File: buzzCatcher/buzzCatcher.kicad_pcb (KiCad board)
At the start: 2 copper layers, 150 x 100 mm, 30 parts, among them IC1 CD4043BE-NG, IC2 COM-16473, IC3 CD74HCT173E, IC4 CD4072BE, IC5 SN74LS04N, IC6 SN74LS21NE4, J1 154-UL6661, J2 154-UL6661, J3 154-UL6661, J4 154-UL6661, J5 USB4130-GF-C, Q1 BS170, SW1 SW_Push

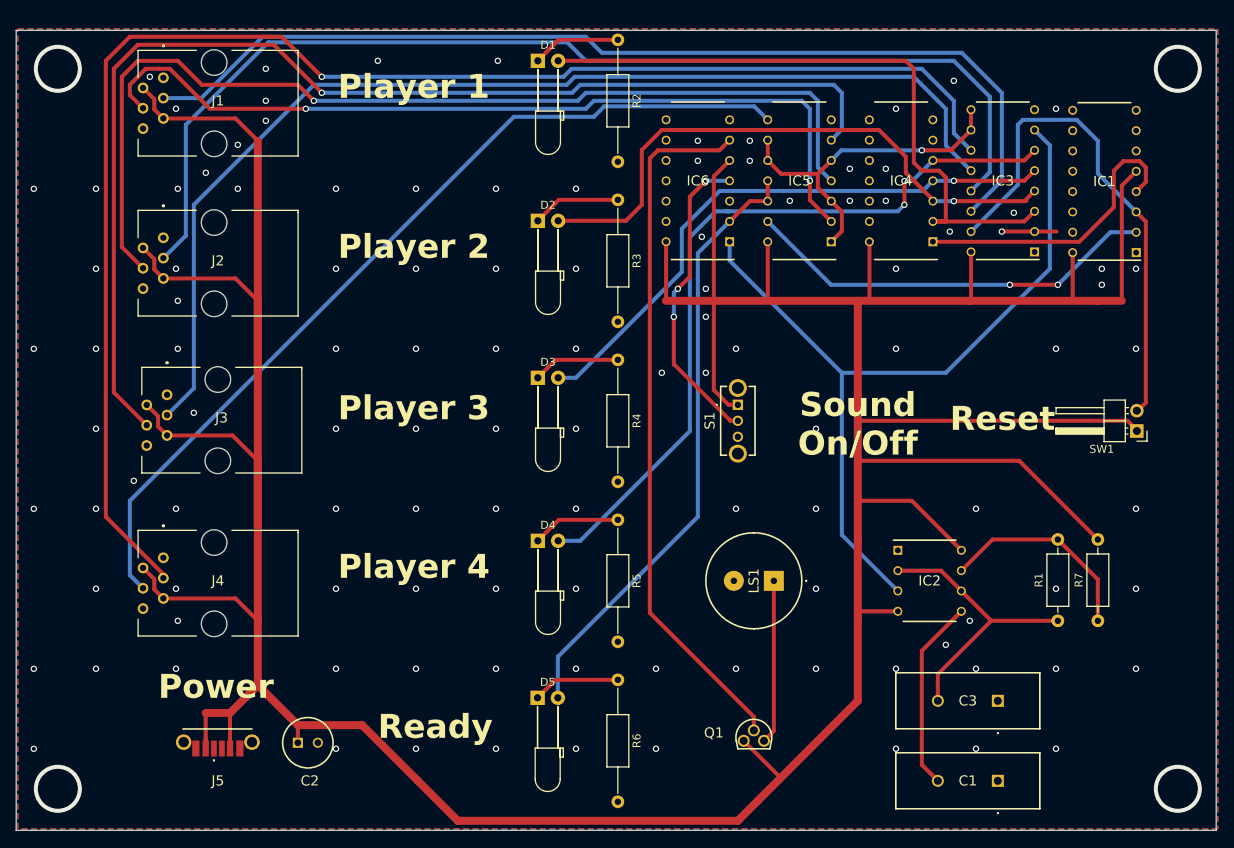
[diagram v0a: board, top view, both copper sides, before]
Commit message: Smaller and cheaper
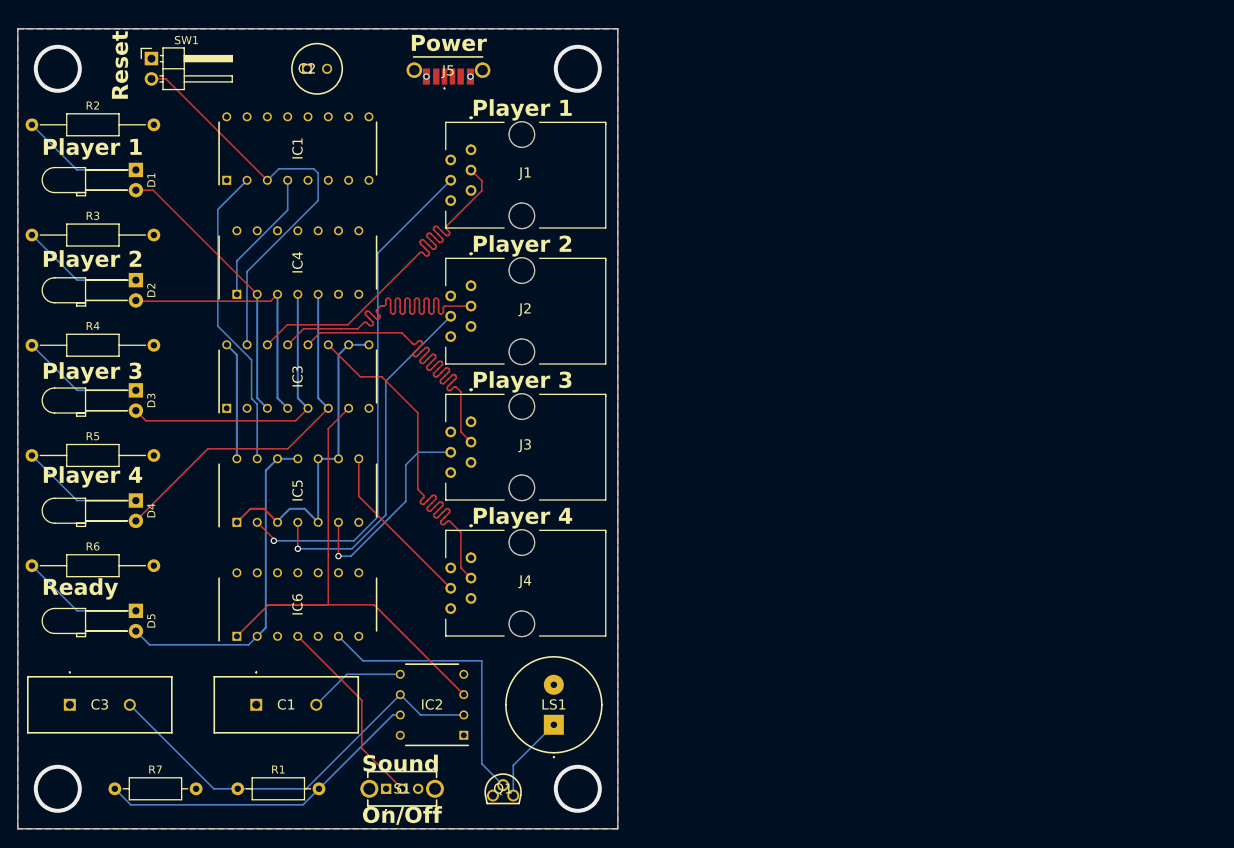
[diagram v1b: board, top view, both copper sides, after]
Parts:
- moved SW1 131.7 mm to (66.7, 53.7), turned to 0 degrees
- moved R7 124.7 mm to (62.1, 145.0), turned to 0 degrees
- moved C3 116.0 mm to (56.5, 134.5), turned to 0 degrees
- moved R1 104.6 mm to (77.5, 145.0), turned to 0 degrees
- moved IC1 100.9 mm to (85.0, 65.0), turned to 90 degrees
- moved C1 93.2 mm to (79.8, 134.5), turned to 0 degrees
- moved IC3 91.5 mm to (85.0, 93.5), turned to 90 degrees
- moved J5 88.8 mm to (103.8, 55.0)
- moved C2 84.3 mm to (86.2, 55.0)
- moved IC4 76.1 mm to (85.0, 79.2), turned to 90 degrees
- moved R6 74.6 mm to (51.8, 117.1), turned to 0 degrees
- moved R2 74.0 mm to (51.8, 62.0), turned to 0 degrees
- moved IC5 73.7 mm to (85.0, 107.7), turned to 90 degrees
- moved R5 73.7 mm to (51.8, 103.3), turned to 0 degrees
- moved R3 73.4 mm to (51.8, 75.8), turned to 0 degrees
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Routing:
- net /Vbus_5V: track 565.0 -> 14.8 mm
- net /trigger_4: track 186.1 -> 49.8 mm, vias 1 -> 0
- net Net-(IC5-3Y): track 148.3 -> 26.3 mm
- net Net-(IC5-4Y): track 112.5 -> 20.9 mm
- net /trigger_3: track 139.0 -> 49.8 mm
- net /trigger_2: track 138.2 -> 50.2 mm
- net Net-(IC5-2Y): track 126.4 -> 44.2 mm
- net /trigger_1: track 127.3 -> 49.8 mm
- net Net-(IC6-1Y): track 87.8 -> 35.8 mm
- net Net-(D4-A): track 96.2 -> 44.7 mm, vias 2 -> 0
- net Net-(D1-A): track 81.7 -> 35.3 mm
- net Net-(IC5-1Y): track 107.5 -> 63.3 mm, vias 2 -> 1
- net Net-(D2-A): track 73.6 -> 33.3 mm, vias 1 -> 0
- net Net-(D3-A): track 73.4 -> 37.5 mm, vias 1 -> 0
- net /listening: track 76.8 -> 42.1 mm
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- added copper zone on F.Cu, net /Vbus_5V
- removed copper zone on F.Cu, net GND
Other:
- board size 150 x 100 mm -> 75 x 100 mm

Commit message: More compact draft
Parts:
- moved IC2 32.9 mm to (70.0, 143.0), turned to 90 degrees
- moved Q1 26.7 mm to (82.7, 145.3)
- moved LS1 19.0 mm to (98.0, 138.0)
- moved S1 17.1 mm to (81.5, 136.0)
- moved R1 17.1 mm to (64.4, 134.0)
- moved R7 15.3 mm to (51.4, 134.0)
- moved J1 11.5 mm to (95.2, 65.6)
- moved J2 11.5 mm to (95.2, 82.6)
- moved J3 11.5 mm to (95.2, 99.6)
- moved J4 11.5 mm to (95.2, 116.6)
- moved J5 8.83 mm to (95.0, 54.8)
- moved IC6 8.82 mm to (79.0, 115.5)
- moved C1 8.56 mm to (76.8, 126.5)
- moved C3 8.00 mm to (56.5, 126.5)
- moved IC5 7.63 mm to (79.0, 103.0)
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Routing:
- net GND: track 0.00 -> 60.0 mm, vias 6 -> 22
- net Net-(IC2-THRES): track 52.0 -> 25.6 mm
- net Net-(IC5-2Y): track 44.2 -> 26.2 mm, vias 1 -> 0
- net Net-(IC5-1Y): track 63.3 -> 45.3 mm, vias 1 -> 0
- net Net-(IC5-3Y): track 26.3 -> 10.0 mm, vias 1 -> 0
- net /Vbus_5V: track 14.8 -> 0.00 mm
- net Net-(IC2-DISCH): track 41.2 -> 27.5 mm
- net Net-(IC1-S1): track 16.9 -> 26.7 mm
- net Net-(IC5-4Y): track 20.9 -> 29.4 mm
- net Net-(IC2-OUT): track 67.7 -> 59.3 mm
- net Net-(D3-A): track 37.5 -> 29.6 mm
- net /listening_state*: track 38.4 -> 31.0 mm
- net /reset_button: track 52.0 -> 44.8 mm
- net Net-(D4-A): track 44.7 -> 37.5 mm
- net Net-(IC6-1Y): track 35.8 -> 29.1 mm
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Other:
- board size 75 x 100 mm -> 63 x 100 mm

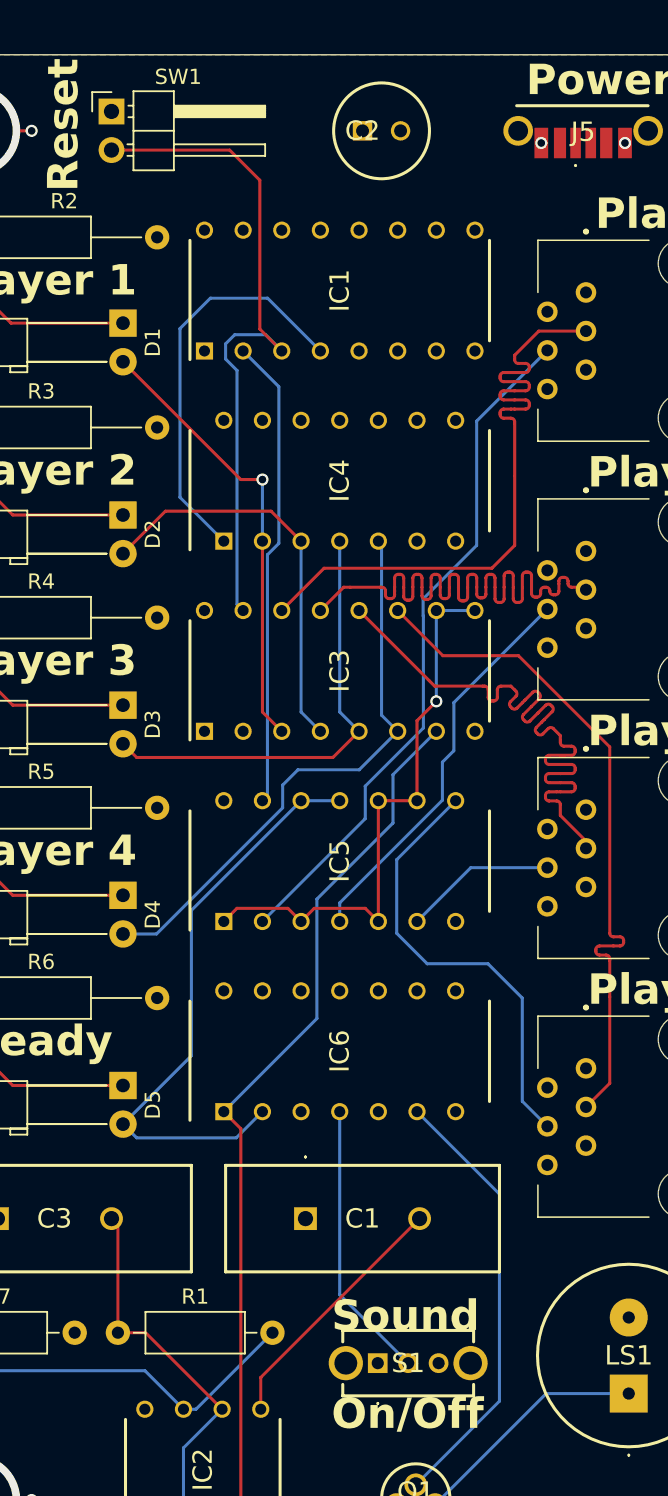
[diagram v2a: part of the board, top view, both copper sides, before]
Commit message: Added handle parts
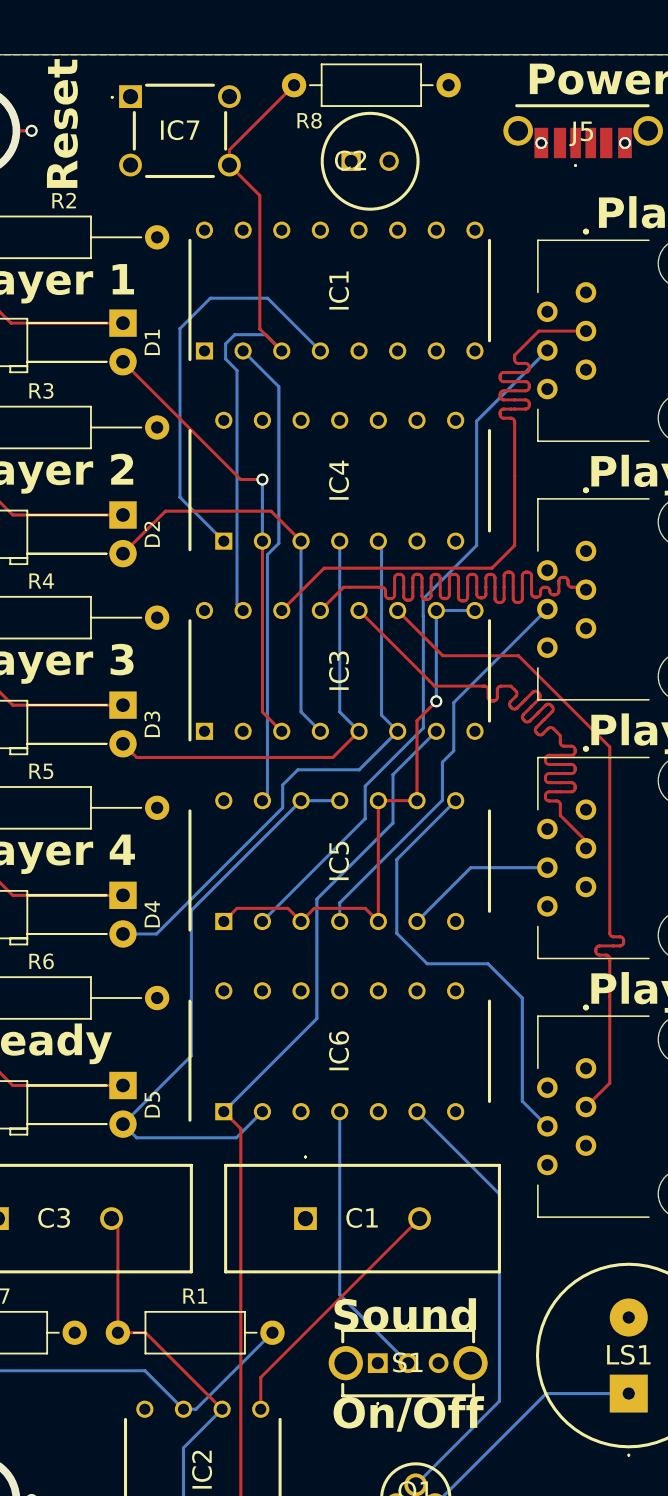
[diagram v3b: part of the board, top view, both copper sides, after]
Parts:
- removed SW1: SW_Push, Connector_PinHeader_2.54mm:PinHeader_1x02_P2.54mm_Horizontal
- added IC7: TS02-66-60-BK-100-SCR-D, SamacSys_PCB_Library:TS026660BK100SCRD, F.Cu at (65.2, 52.7)
- added R8: 110k, Resistor_THT:R_Axial_DIN0207_L6.3mm_D2.5mm_P10.16mm_Horizontal, F.Cu at (86.2, 52.0)
- moved C2 2.14 mm to (79.8, 57.0)
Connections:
- J1 pad 2: /Vbus_5V -> GND
- J2 pad 2: /Vbus_5V -> GND
- J3 pad 2: /Vbus_5V -> GND
- J4 pad 2: /Vbus_5V -> GND
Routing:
- net /reset_button: track 44.8 -> 43.0 mm
